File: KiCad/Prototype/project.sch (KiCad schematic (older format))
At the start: 74 parts, among them J1 Barrel_Jack, J10 POT 2, J11 POT 3, J12 POT 4, J13 POT 5, J14 PRESSURE, J15 MIDI IN, J16 MIDI OUT, J17 POT 6, J18 POT 7, J19 POT 8, J2 USB_B, J20 TTL MIDI, J3 ICSP, J4 BANK 0..7, J5 BANK 8..15, J6 EXPRESSION, J7 SUSTAIN, J8 PD6/ADC9/SPEAKER, J9 POT 1, Q1 PMV48XP,215, SW1 RESET, U1 74LS75, U10 HCPL-0600, U2 LMV358, U3 AMS1117-5.0, U4 ATMEGA32U4-AU, U5 74HC138, U6 74HC138, U7 74HC238, U8 74HC238, U9 74HC04, Y1 16 Mhz

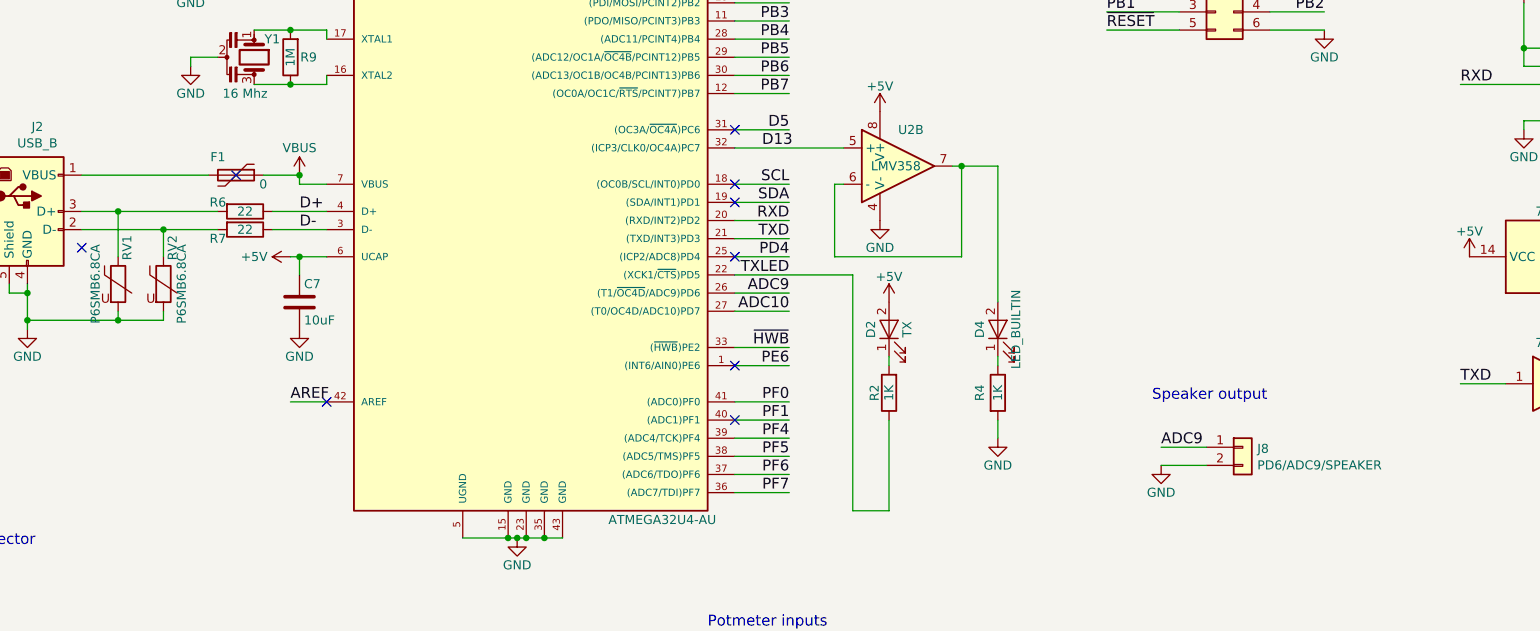
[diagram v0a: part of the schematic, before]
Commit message: electrical changes for analog mux
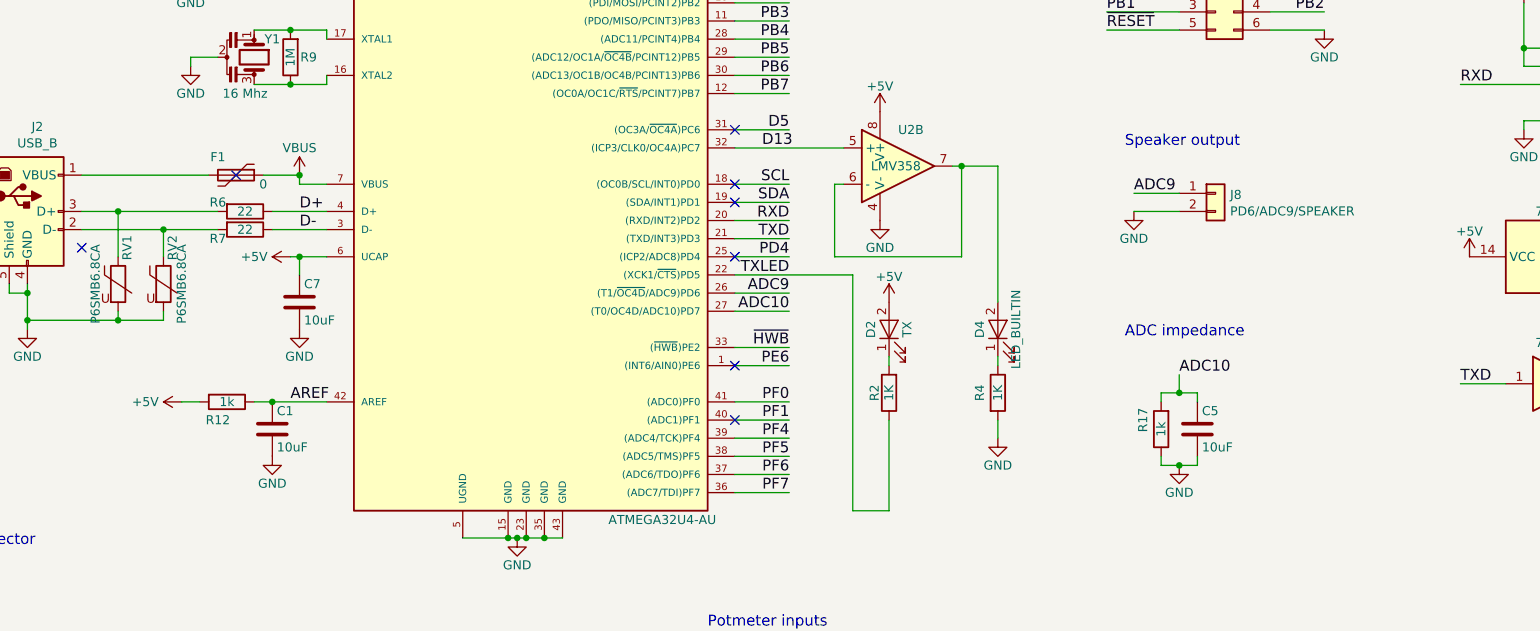
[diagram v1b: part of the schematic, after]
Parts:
- added C1, C5: 10uF, footprints:C_1206_HandSoldering, symbol project:C
- added R12, R17: 1k, footprints:R_0805_HandSoldering, symbol project:R
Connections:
- net +5V: now also R12.2
- net ADC10: now also C5.1, R17.2
- net AREF: now also C1.1, R12.1
- net GND: now also C1.2, C5.2, R17.1
- no-connect marks 25 -> 24
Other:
- note added: "ADC impedance"
- moved on the sheet: J8
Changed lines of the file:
@@
 Connection ~ 6100 2900
-Wire Wire Line
-	6250 3700 6050 3700
 Wire Wire Line
 	6100 2500 6250 2500
@@
 L Connector_Generic:Conn_01x02 J8
 U 1 1 5EC2996C
-P 11300 3950
-F 0 "J8" H 11380 3942 50  0000 L CNN
-F 1 "PD6/ADC9/SPEAKER" H 11380 3851 50  0000 L CNN
-F 2 "footprints:Molex_KK-254_AE-6410-02A_1x02_P2.54mm_Vertical" H 11300 3950 50  0001 C CNN
-F 3 "~" H 11300 3950 50  0001 C CNN
-F 4 "571-640454-2" H 11300 3950 50  0001 C CNN "MOUSER"
-	1    11300 3950
-	1    0    0    -1
-$EndComp
-Wire Wire Line
-	11100 3950 10850 3950
-Wire Wire Line
-	11100 4050 10850 4050
+P 11150 2550
+F 0 "J8" H 11230 2542 50  0000 L CNN
+F 1 "PD6/ADC9/SPEAKER" H 11230 2451 50  0000 L CNN
+F 2 "footprints:Molex_KK-254_AE-6410-02A_1x02_P2.54mm_Vertical" H 11150 2550 50  0001 C CNN
+F 3 "~" H 11150 2550 50  0001 C CNN
+F 4 "571-640454-2" H 11150 2550 50  0001 C CNN "MOUSER"
+	1    11150 2550
+	1    0    0    -1
+$EndComp
+Wire Wire Line
+	10950 2550 10700 2550
+Wire Wire Line
+	10950 2650 10700 2650
 $Comp
 L project:GND #PWR054
 U 1 1 5ECF891C
-P 10850 4050
-F 0 "#PWR054" H 10850 3800 50  0001 C CNN
-F 1 "GND" H 10850 3900 50  0000 C CNN
-F 2 "" H 10850 4050 50  0001 C CNN
-F 3 "" H 10850 4050 50  0001 C CNN
-	1    10850 4050
-	1    0    0    -1
-$EndComp
-Text Label 10850 3950 0    60   ~ 0
+P 10700 2650
+F 0 "#PWR054" H 10700 2400 50  0001 C CNN
+F 1 "GND" H 10700 2500 50  0000 C CNN
+F 2 "" H 10700 2650 50  0001 C CNN
+F 3 "" H 10700 2650 50  0001 C CNN
+	1    10700 2650
+	1    0    0    -1
+$EndComp
+Text Label 10700 2550 0    60   ~ 0
 ADC9
-Text Notes 10800 3700 0    60   ~ 0
+Text Notes 10650 2300 0    60   ~ 0
 Speaker output
 $Comp
@@
 NoConn ~ 8500 3800
 NoConn ~ 8500 3500
-NoConn ~ 6250 3700
 $Comp
 L project:PWR_FLAG #FLG0101
@@
 	14400 9450 14750 9450
 Connection ~ 14750 9450
+$Comp
+L project:C C1
+U 1 1 627B15D7
+P 5950 3850
+F 0 "C1" H 5975 3950 50  0000 L CNN
+F 1 "10uF" H 5975 3750 50  0000 L CNN
+F 2 "footprints:C_1206_HandSoldering" H 5988 3700 50  0001 C CNN
+F 3 "" H 5950 3850 50  0001 C CNN
+F 4 "C13585" H 5950 3850 50  0001 C CNN "LCSC"
+	1    5950 3850
+	1    0    0    -1
+$EndComp
+$Comp
+L project:R R12
+U 1 1 627B2258
+P 5700 3700
+F 0 "R12" V 5800 3650 50  0000 C CNN
+F 1 "1k" V 5700 3700 50  0000 C CNN
+F 2 "footprints:R_0805_HandSoldering" V 5630 3700 50  0001 C CNN
+F 3 "" H 5700 3700 50  0001 C CNN
+F 4 "C17561" H 5700 3700 50  0001 C CNN "LCSC"
+	1    5700 3700
+	0    1    1    0
+$EndComp
+$Comp
+L project:+5V #PWR037
+U 1 1 627B27F2
+P 5450 3700
+F 0 "#PWR037" H 5450 3550 50  0001 C CNN
+F 1 "+5V" V 5450 3900 50  0000 C CNN
+F 2 "" H 5450 3700 50  0001 C CNN
+F 3 "" H 5450 3700 50  0001 C CNN
+	1    5450 3700
+	0    -1   -1   0
+$EndComp
+$Comp
+L project:GND #PWR055
+U 1 1 627BC34F
+P 5950 4000
+F 0 "#PWR055" H 5950 3750 50  0001 C CNN
+F 1 "GND" H 5950 3850 50  0000 C CNN
+F 2 "" H 5950 4000 50  0001 C CNN
+F 3 "" H 5950 4000 50  0001 C CNN
+	1    5950 4000
+	1    0    0    -1
+$EndComp
+Wire Wire Line
+	5450 3700 5550 3700
+Wire Wire Line
+	5850 3700 5950 3700
+Connection ~ 5950 3700
+Wire Wire Line
+	5950 3700 6250 3700
+Text Notes 10650 3350 0    60   ~ 0
+ADC impedance
+Text Label 10950 3550 0    60   ~ 0
+ADC10
+$Comp
+L project:R R17
+U 1 1 628920BD
+P 10850 3850
+F 0 "R17" V 10950 3800 50  0000 C CNN
+F 1 "1k" V 10850 3850 50  0000 C CNN
+F 2 "footprints:R_0805_HandSoldering" V 10780 3850 50  0001 C CNN
+F 3 "" H 10850 3850 50  0001 C CNN
+F 4 "C17561" H 10850 3850 50  0001 C CNN "LCSC"
+	1    10850 3850
+	-1   0    0    1
+$EndComp
+$Comp
+L project:C C5
+U 1 1 62892E72
+P 11050 3850
+F 0 "C5" H 11075 3950 50  0000 L CNN
+F 1 "10uF" H 11075 3750 50  0000 L CNN
+F 2 "footprints:C_1206_HandSoldering" H 11088 3700 50  0001 C CNN
+F 3 "" H 11050 3850 50  0001 C CNN
+F 4 "C13585" H 11050 3850 50  0001 C CNN "LCSC"
+	1    11050 3850
+	1    0    0    -1
+$EndComp
+$Comp
+L project:GND #PWR056
+U 1 1 62893A0C
+P 10950 4050
+F 0 "#PWR056" H 10950 3800 50  0001 C CNN
+F 1 "GND" H 10950 3900 50  0000 C CNN
+F 2 "" H 10950 4050 50  0001 C CNN
+F 3 "" H 10950 4050 50  0001 C CNN
+	1    10950 4050
+	1    0    0    -1
+$EndComp
+Wire Wire Line
+	10850 3700 10850 3650
+Wire Wire Line
+	10850 3650 10950 3650
+Wire Wire Line
+	11050 3650 11050 3700
+Wire Wire Line
+	10950 3550 10950 3650
+Connection ~ 10950 3650
+Wire Wire Line
+	10950 3650 11050 3650
+Wire Wire Line
+	10850 4000 10850 4050
+Wire Wire Line
+	10850 4050 10950 4050
+Wire Wire Line
+	11050 4000 11050 4050
+Wire Wire Line
+	11050 4050 10950 4050
+Connection ~ 10950 4050
 $EndSCHEMATC
